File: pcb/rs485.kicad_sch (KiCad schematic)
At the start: 8 parts, among them J13 Conn_01x03_Pin, J14 Conn_01x03_Pin, U10 CPDV5-5V0U, U11 ST3485EB

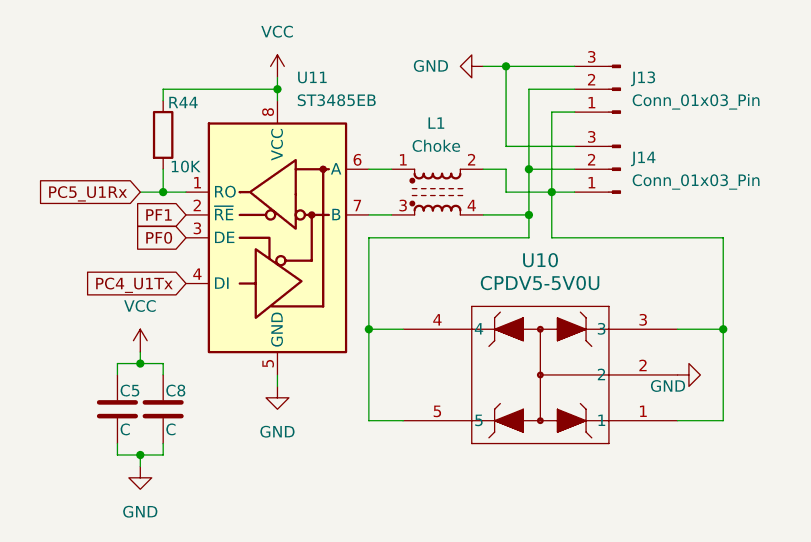
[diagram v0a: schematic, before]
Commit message: Add new IMU revision and more info in readme
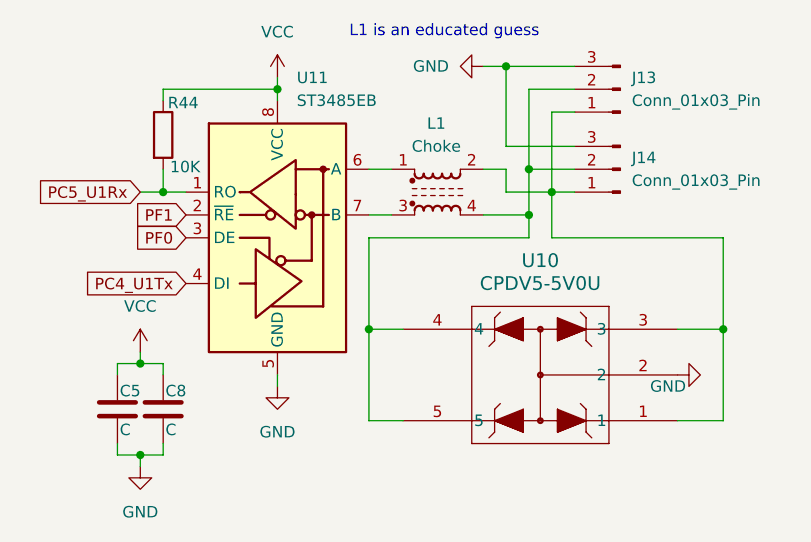
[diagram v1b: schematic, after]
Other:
- note added: "L1 is an educated guess"
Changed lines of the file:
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@@
 	(generator_version "9.0")
 	(paper "A4")
+	(text "L1 is an educated guess"
+		(exclude_from_sim no)
+		(at 145.542 64.77 0)
+		(effects
+			(font
+				(size 1.27 1.27)
+			)
+		)
+	)
 	(junction
 		(at 127 71.12)
